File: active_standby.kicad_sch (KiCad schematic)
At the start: 20 parts, among them Q10 BSS138, Q11 BSS138, Q2 BSS138, Q8 BSS138, Q9 BSS138, U24 SN3257QDYYRQ1, U30 SN3257QDYYRQ1

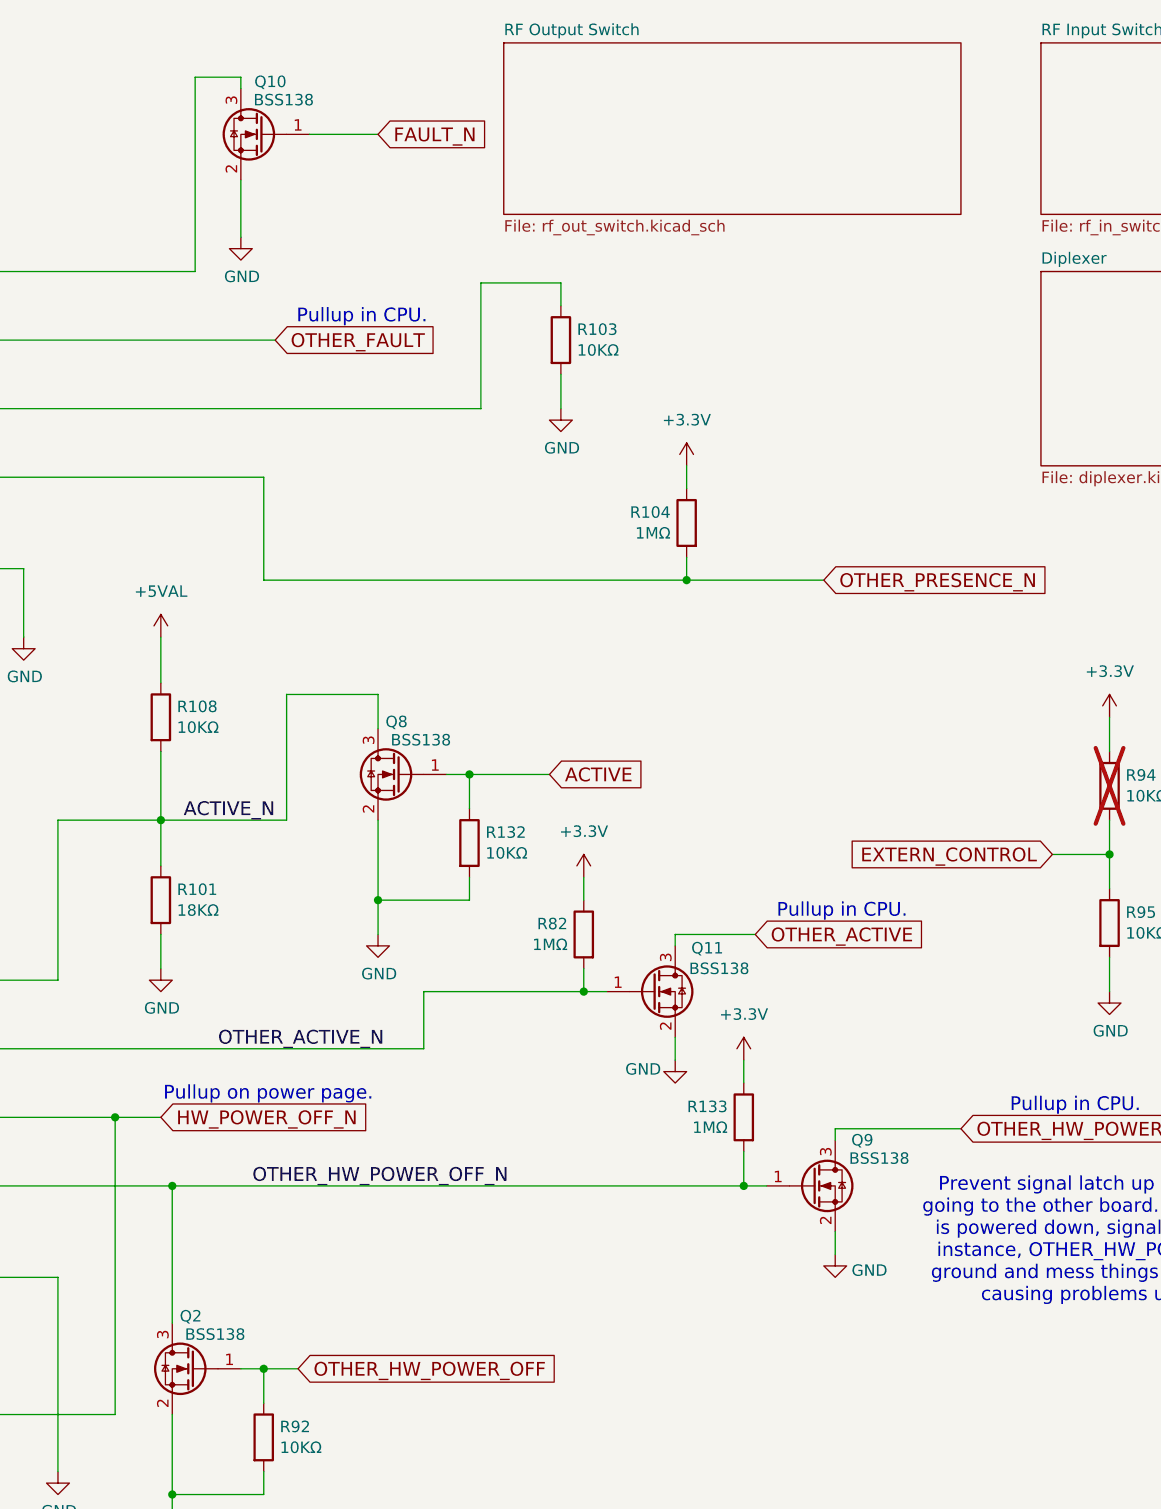
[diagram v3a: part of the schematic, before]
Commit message: Parts replacements for out of stock parts
Signed-off-by: Corey Minyard <corey@minyard.net>
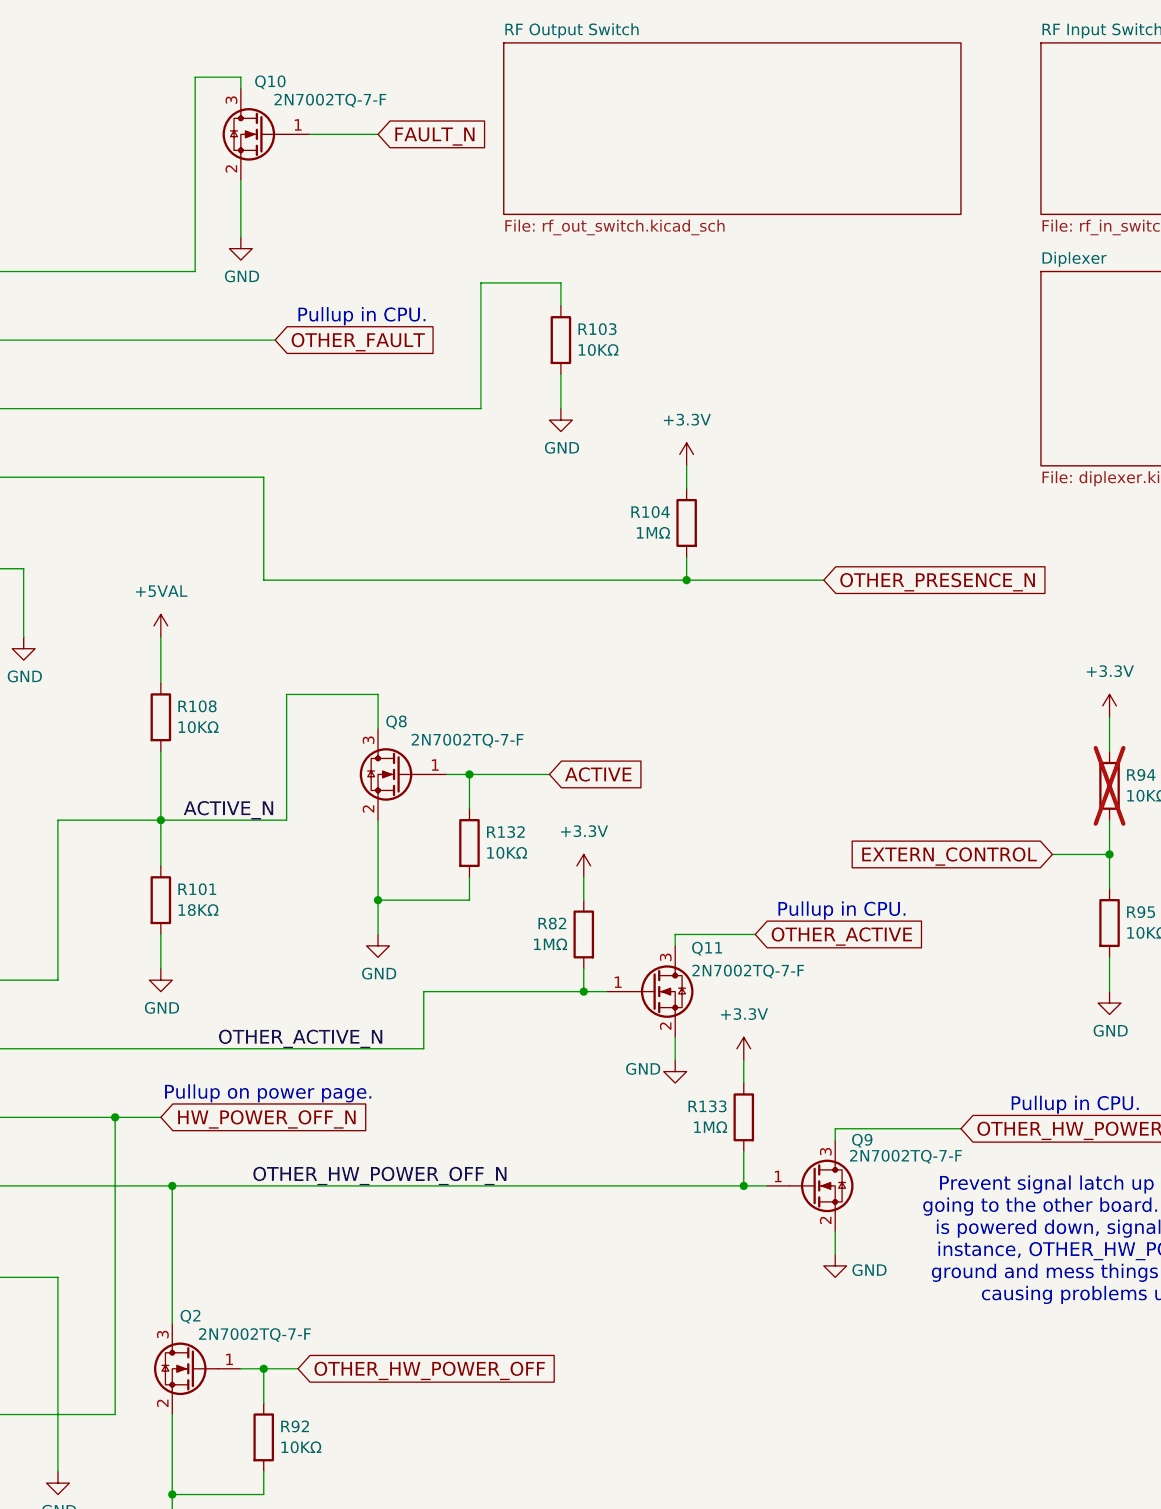
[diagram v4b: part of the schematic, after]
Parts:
- Q10, Q11, Q2, Q8, Q9: value BSS138 -> 2N7002TQ-7-F; symbol Transistor_FET:BSS138 -> PACSAT_DEV_misc:2N7002TQ-7-F
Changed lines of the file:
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@@
 	)
 	(symbol
-		(lib_id "Transistor_FET:BSS138")
+		(lib_id "PACSAT_DEV_misc:2N7002TQ-7-F")
 		(at 133.35 168.91 0)
 		(mirror y)
@@
 			)
 		)
-		(property "Value" "BSS138"
-			(at 138.938 165.1 0)
+		(property "Value" "2N7002TQ-7-F"
+			(at 146.304 165.1 0)
 			(effects
 				(font
@@
 			)
 		)
-		(property "Datasheet" "https://www.onsemi.com/pub/Collateral/BSS138-D.PDF"
+		(property "Datasheet" "https://www.diodes.com/assets/Datasheets/2N7002TQ.pdf"
 			(at 128.27 172.72 0)
 			(effects
@@
 			)
 		)
-		(property "Description" "50V Vds, 0.22A Id, N-Channel MOSFET, SOT-23"
+		(property "Description" "MOSFET N-CH 60V 115MA SOT523"
 			(at 133.35 168.91 0)
 			(effects
@@
 	)
 	(symbol
-		(lib_id "Transistor_FET:BSS138")
+		(lib_id "PACSAT_DEV_misc:2N7002TQ-7-F")
 		(at 140.97 31.75 0)
 		(mirror y)
@@
 			)
 		)
-		(property "Value" "BSS138"
-			(at 146.558 27.94 0)
+		(property "Value" "2N7002TQ-7-F"
+			(at 154.686 27.94 0)
 			(effects
 				(font
@@
 			)
 		)
-		(property "Datasheet" "https://www.onsemi.com/pub/Collateral/BSS138-D.PDF"
+		(property "Datasheet" "https://www.diodes.com/assets/Datasheets/2N7002TQ.pdf"
 			(at 135.89 35.56 0)
 			(effects
@@
 			)
 		)
-		(property "Description" "50V Vds, 0.22A Id, N-Channel MOSFET, SOT-23"
+		(property "Description" "MOSFET N-CH 60V 115MA SOT523"
 			(at 140.97 31.75 0)
 			(effects
@@
 	)
 	(symbol
-		(lib_id "Transistor_FET:BSS138")
+		(lib_id "PACSAT_DEV_misc:2N7002TQ-7-F")
 		(at 201.93 148.59 0)
 		(unit 1)
@@
 			)
 		)
-		(property "Value" "BSS138"
-			(at 205.994 145.542 0)
+		(property "Value" "2N7002TQ-7-F"
+			(at 205.994 145.288 0)
 			(effects
 				(font
@@
 			)
 		)
-		(property "Datasheet" "https://www.onsemi.com/pub/Collateral/BSS138-D.PDF"
+		(property "Datasheet" "https://www.diodes.com/assets/Datasheets/2N7002TQ.pdf"
 			(at 207.01 152.4 0)
 			(effects
@@
 			)
 		)
-		(property "Description" "50V Vds, 0.22A Id, N-Channel MOSFET, SOT-23"
+		(property "Description" "MOSFET N-CH 60V 115MA SOT523"
 			(at 201.93 148.59 0)
 			(effects
@@
 	)
 	(symbol
-		(lib_id "Transistor_FET:BSS138")
+		(lib_id "PACSAT_DEV_misc:2N7002TQ-7-F")
 		(at 184.15 127 0)
 		(unit 1)
@@
 			)
 		)
-		(property "Value" "BSS138"
-			(at 188.214 124.46 0)
+		(property "Value" "2N7002TQ-7-F"
+			(at 188.468 124.714 0)
 			(effects
 				(font
@@
 			)
 		)
-		(property "Datasheet" "https://www.onsemi.com/pub/Collateral/BSS138-D.PDF"
+		(property "Datasheet" "https://www.diodes.com/assets/Datasheets/2N7002TQ.pdf"
 			(at 189.23 130.81 0)
 			(effects
@@
 			)
 		)
-		(property "Description" "50V Vds, 0.22A Id, N-Channel MOSFET, SOT-23"
+		(property "Description" "MOSFET N-CH 60V 115MA SOT523"
 			(at 184.15 127 0)
 			(effects
@@
 	)
 	(symbol
-		(lib_id "Transistor_FET:BSS138")
+		(lib_id "PACSAT_DEV_misc:2N7002TQ-7-F")
 		(at 156.21 102.87 0)
 		(mirror y)
@@
 			)
 		)
-		(property "Value" "BSS138"
-			(at 161.798 99.06 0)
+		(property "Value" "2N7002TQ-7-F"
+			(at 169.926 99.06 0)
 			(effects
 				(font
@@
 			)
 		)
-		(property "Datasheet" "https://www.onsemi.com/pub/Collateral/BSS138-D.PDF"
+		(property "Datasheet" "https://www.diodes.com/assets/Datasheets/2N7002TQ.pdf"
 			(at 151.13 106.68 0)
 			(effects
@@
 			)
 		)
-		(property "Description" "50V Vds, 0.22A Id, N-Channel MOSFET, SOT-23"
+		(property "Description" "MOSFET N-CH 60V 115MA SOT523"
 			(at 156.21 102.87 0)
 			(effects

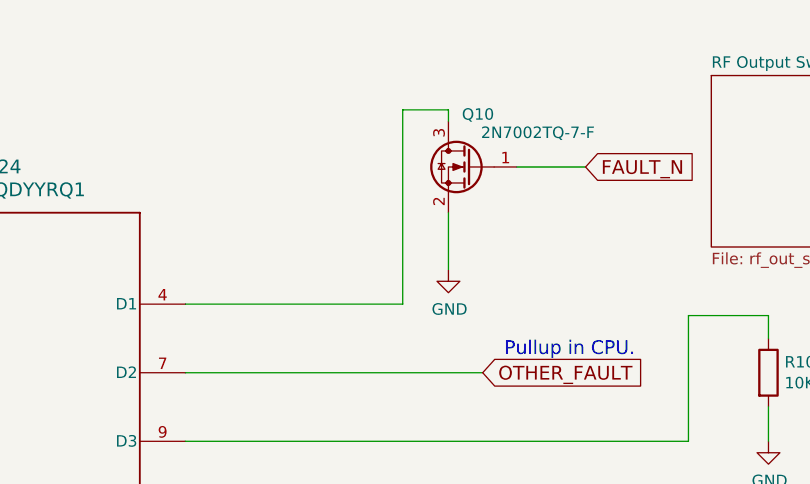
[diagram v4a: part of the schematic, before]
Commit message: Add DNI pull resistors to FAULT_N
In case they are needed.

Signed-off-by: Corey Minyard <corey@minyard.net>
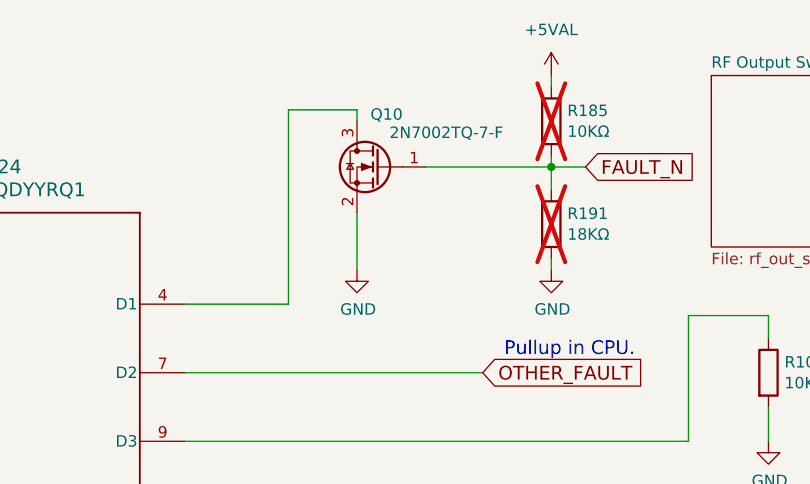
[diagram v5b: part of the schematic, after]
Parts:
- added R185: 10KΩ, Resistor_SMD:R_0402_1005Metric_Pad0.72x0.64mm_HandSolder, symbol Device:R
- added R191: 18KΩ, Resistor_SMD:R_0402_1005Metric_Pad0.72x0.64mm_HandSolder, symbol Device:R
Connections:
- net +5VAL: now also R185.1
- net FAULT_N: now also R185.2, R191.1
- net GND: now also R191.2
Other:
- moved on the sheet: Q10
